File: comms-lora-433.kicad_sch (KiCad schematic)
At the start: 3 parts, among them J3 Conn_Coaxial_Small, U3 RFM95W-915S2

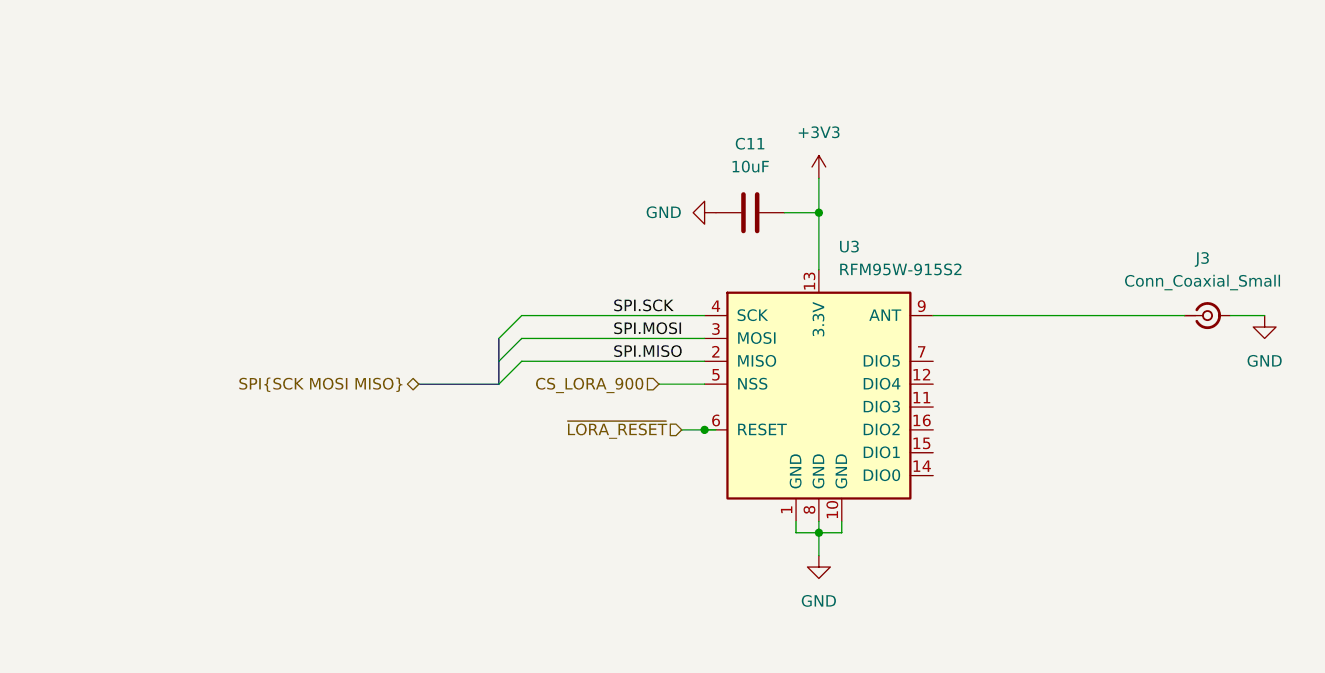
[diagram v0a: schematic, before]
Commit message: Adding symbols information
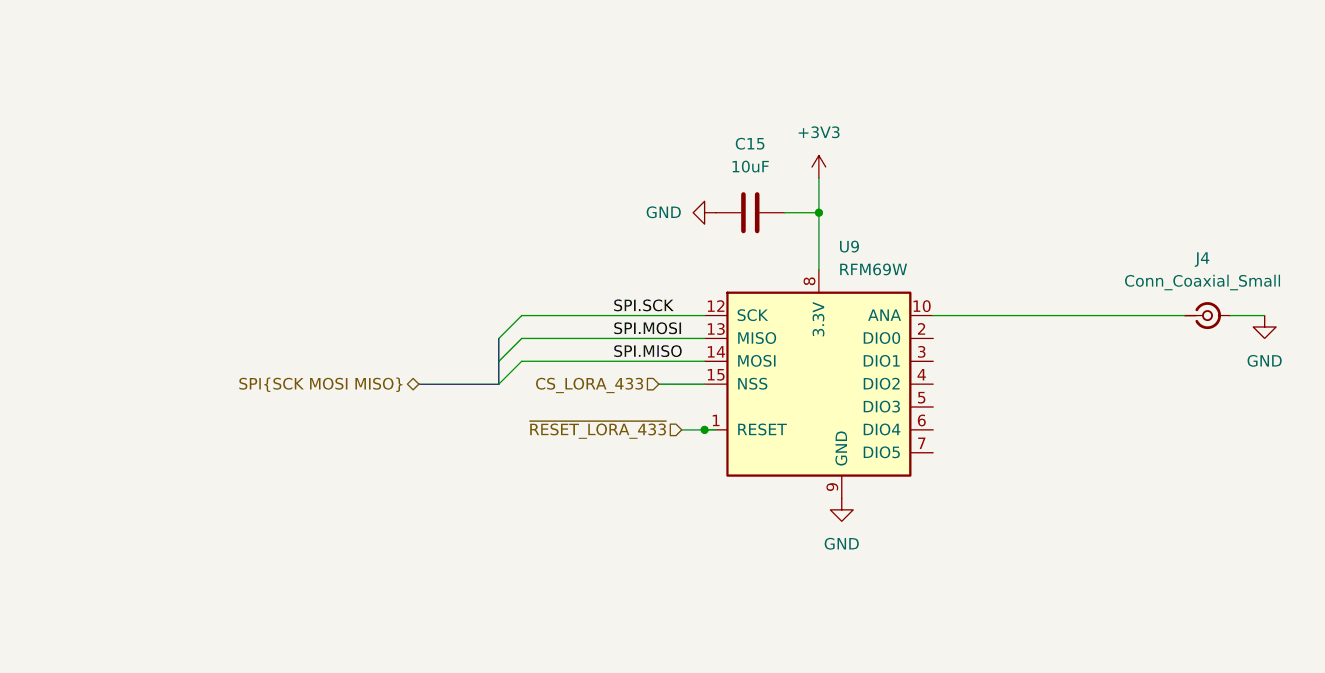
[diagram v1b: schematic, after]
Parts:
- removed U3: RFM95W-915S2, symbol RF_Module:RFM95W-915S2
- added U9: RFM69W, RF_Module:HOPERF_RFM69HW, symbol RF_Module:RFM69W
- renumbered C11 to C15, J3 to J4
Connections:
- net +3V3: now also U9.8 (3.3V)
- net GND: now also U9.11 (GND), U9.9 (GND)
- net SPI.MISO: now also U9.14 (MOSI)
- net SPI.MOSI: now also U9.13 (MISO)
- net SPI.SCK: now also U9.12 (SCK)
- net at J4.1 (In): now also U9.10 (ANA)
- new net CS_LORA_433: U9.15 (NSS)
- new net ~{RESET_LORA_433}: U9.1 (RESET)
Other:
- company: (none) -> catbranchman

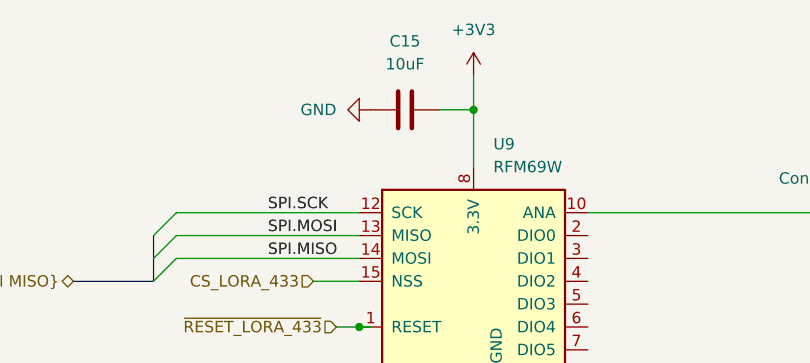
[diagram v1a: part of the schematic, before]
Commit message: Adding rest of schematic
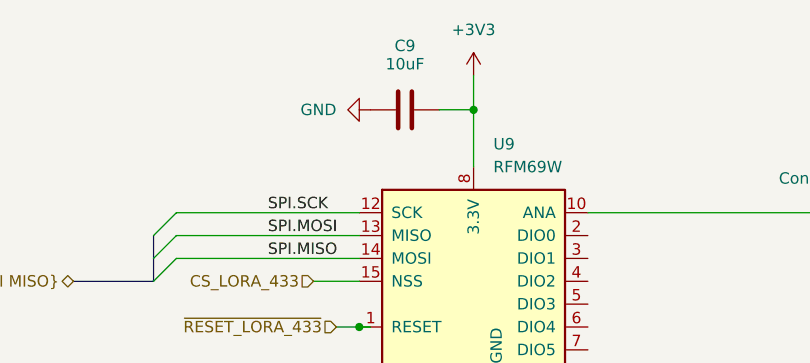
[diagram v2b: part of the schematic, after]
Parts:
- removed C15: 10uF, symbol Device:C
- added C9: 10uF, Inductor_SMD:L_0805_2012Metric, symbol Device:C
- J4: footprint (none) -> Connector_Coaxial:U.FL_Molex_MCRF_73412-0110_Vertical; Mfr (none) -> Molex; Mfr P/N (none) -> 0734120110; Supplier_1 (none) -> Digikey; Supplier_1 P/N (none) -> WM5587CT-ND; Supplier_1 Price @ Qty (none) -> $0.38945; Supplier_1 Unit Price (none) -> $0.94000
- U9: Mfr (none) -> Adafruit; Mfr P/N (none) -> 3073; Supplier_1 (none) -> Adafruit; Supplier_1 P/N (none) -> 3073; Supplier_1 Price @ Qty (none) -> $15.96; Supplier_1 Unit Price (none) -> $19.95
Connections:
- net +3V3: now also C9.2
- net GND: now also C9.1

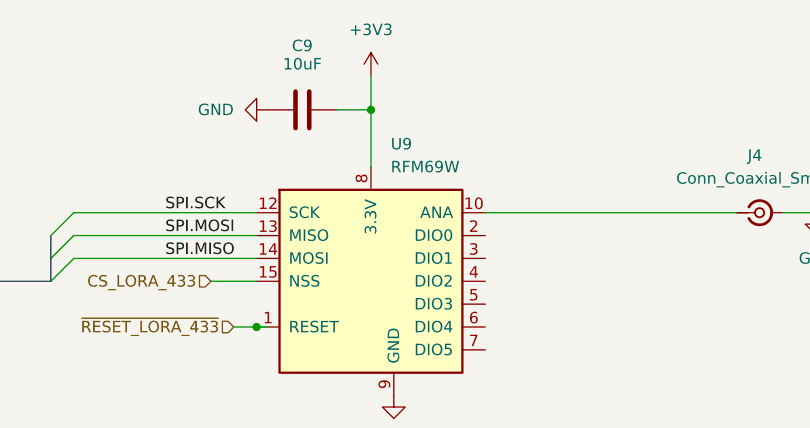
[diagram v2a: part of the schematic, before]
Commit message: Fixing footprint imports
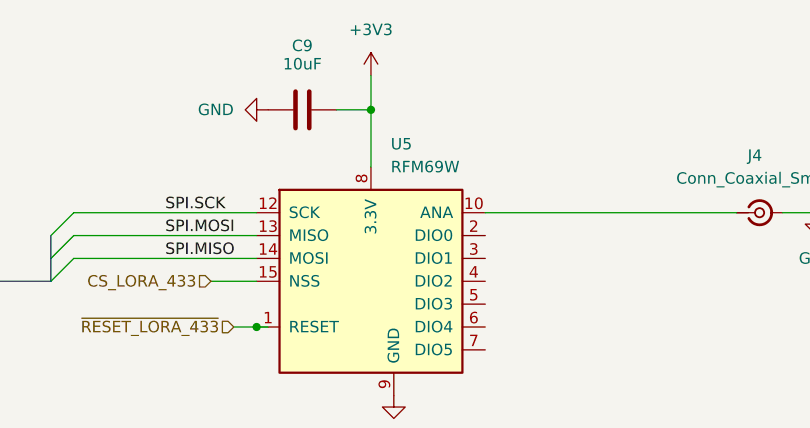
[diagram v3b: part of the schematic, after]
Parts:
- renumbered U9 to U5
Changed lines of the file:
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@@
 		)
 	)
-	(label "SPI.MOSI"
-		(at 121.92 92.71 0)
+	(label "SPI.MISO"
+		(at 121.92 95.25 0)
 		(fields_autoplaced yes)
 		(effects
@@
 		)
 	)
-	(label "SPI.MISO"
-		(at 121.92 95.25 0)
+	(label "SPI.MOSI"
+		(at 121.92 92.71 0)
 		(fields_autoplaced yes)
 		(effects
@@
 		)
 	)
+	(hierarchical_label "~{RESET_LORA_433}"
+		(shape input)
+		(at 129.54 102.87 180)
+		(fields_autoplaced yes)
+		(effects
+			(font
+				(size 1.27 1.27)
+			)
+			(justify right)
+		)
+	)
 	(hierarchical_label "CS_LORA_433"
 		(shape input)
 		(at 127 97.79 180)
-		(fields_autoplaced yes)
-		(effects
-			(font
-				(size 1.27 1.27)
-			)
-			(justify right)
-		)
-	)
-	(hierarchical_label "~{RESET_LORA_433}"
-		(shape input)
-		(at 129.54 102.87 180)
 		(fields_autoplaced yes)
 		(effects
@@
 		(dnp no)
 		(fields_autoplaced yes)
-		(property "Reference" "U9"
+		(property "Reference" "U5"
 			(at 146.9741 82.55 0)
 			(effects
@@
 			(project ""
 				(path "/1c59de6a-87fe-4223-8898-4b0383164a31/27e0c772-2e0b-4398-8c51-a65e2e356334"
-					(reference "U9")
+					(reference "U5")
+					(unit 1)
+				)
+			)
+		)
+	)
+	(symbol
+		(lib_id "power:GND")
+		(at 133.35 78.74 270)
+		(unit 1)
+		(exclude_from_sim no)
+		(in_bom yes)
+		(on_board yes)
+		(dnp no)
+		(fields_autoplaced yes)
+		(property "Reference" "#PWR058"
+			(at 127 78.74 0)
+			(effects
+				(font
+					(size 1.27 1.27)
+				)
+				(hide yes)
+			)
+		)
+		(property "Value" "GND"
+			(at 129.54 78.7399 90)
+			(effects
+				(font
+					(size 1.27 1.27)
+				)
+				(justify right)
+			)
+		)
+		(property "Footprint" ""
+			(at 133.35 78.74 0)
+			(effects
+				(font
+					(size 1.27 1.27)
+				)
+				(hide yes)
+			)
+		)
+		(property "Datasheet" ""
+			(at 133.35 78.74 0)
+			(effects
+				(font
+					(size 1.27 1.27)
+				)
+				(hide yes)
+			)
+		)
+		(property "Description" "Power symbol creates a global label with name \"GND\" , ground"
+			(at 133.35 78.74 0)
+			(effects
+				(font
+					(size 1.27 1.27)
+				)
+				(hide yes)
+			)
+		)
+		(pin "1"
+		)
+		(instances
+			(project "roamer"
+				(path "/1c59de6a-87fe-4223-8898-4b0383164a31/27e0c772-2e0b-4398-8c51-a65e2e356334"
+					(reference "#PWR058")
 					(unit 1)
 				)
@@
 	)
 	(symbol
-		(lib_id "power:GND")
-		(at 133.35 78.74 270)
-		(unit 1)
-		(exclude_from_sim no)
-		(in_bom yes)
-		(on_board yes)
-		(dnp no)
-		(fields_autoplaced yes)
-		(property "Reference" "#PWR058"
-			(at 127 78.74 0)
-			(effects
-				(font
-					(size 1.27 1.27)
-				)
-				(hide yes)
-			)
-		)
-		(property "Value" "GND"
-			(at 129.54 78.7399 90)
-			(effects
-				(font
-					(size 1.27 1.27)
-				)
-				(justify right)
-			)
-		)
-		(property "Footprint" ""
-			(at 133.35 78.74 0)
-			(effects
-				(font
-					(size 1.27 1.27)
-				)
-				(hide yes)
-			)
-		)
-		(property "Datasheet" ""
-			(at 133.35 78.74 0)
-			(effects
-				(font
-					(size 1.27 1.27)
-				)
-				(hide yes)
-			)
-		)
-		(property "Description" "Power symbol creates a global label with name \"GND\" , ground"
-			(at 133.35 78.74 0)
-			(effects
-				(font
-					(size 1.27 1.27)
-				)
-				(hide yes)
-			)
-		)
-		(pin "1"
-		)
-		(instances
-			(project "roamer"
-				(path "/1c59de6a-87fe-4223-8898-4b0383164a31/27e0c772-2e0b-4398-8c51-a65e2e356334"
-					(reference "#PWR058")
-					(unit 1)
-				)
-			)
-		)
-	)
-	(symbol
 		(lib_id "power:+3V3")
 		(at 144.78 74.93 0)
@@
 				(path "/1c59de6a-87fe-4223-8898-4b0383164a31/27e0c772-2e0b-4398-8c51-a65e2e356334"
 					(reference "#PWR059")
+					(unit 1)
+				)
+			)
+		)
+	)
+	(symbol
+		(lib_id "power:GND")
+		(at 194.31 90.17 0)
+		(unit 1)
+		(exclude_from_sim no)
+		(in_bom yes)
+		(on_board yes)
+		(dnp no)
+		(fields_autoplaced yes)
+		(property "Reference" "#PWR061"
+			(at 194.31 96.52 0)
+			(effects
+				(font
+					(size 1.27 1.27)
+				)
+				(hide yes)
+			)
+		)
+		(property "Value" "GND"
+			(at 194.31 95.25 0)
+			(effects
+				(font
+					(size 1.27 1.27)
+				)
+			)
+		)
+		(property "Footprint" ""
+			(at 194.31 90.17 0)
+			(effects
+				(font
+					(size 1.27 1.27)
+				)
+				(hide yes)
+			)
+		)
+		(property "Datasheet" ""
+			(at 194.31 90.17 0)
+			(effects
+				(font
+					(size 1.27 1.27)
+				)
+				(hide yes)
+			)
+		)
+		(property "Description" "Power symbol creates a global label with name \"GND\" , ground"
+			(at 194.31 90.17 0)
+			(effects
+				(font
+					(size 1.27 1.27)
+				)
+				(hide yes)
+			)
+		)
+		(pin "1"
+		)
+		(instances
+			(project "roamer"
+				(path "/1c59de6a-87fe-4223-8898-4b0383164a31/27e0c772-2e0b-4398-8c51-a65e2e356334"
+					(reference "#PWR061")
 					(unit 1)
 				)
@@
 					(unit 1)
 				)
-			)
-		)
-	)
-	(symbol
-		(lib_id "power:GND")
-		(at 194.31 90.17 0)
-		(unit 1)
-		(exclude_from_sim no)
-		(in_bom yes)
-		(on_board yes)
-		(dnp no)
-		(fields_autoplaced yes)
-		(property "Reference" "#PWR061"
-			(at 194.31 96.52 0)
-			(effects
-				(font
-					(size 1.27 1.27)
-				)
-				(hide yes)
-			)
-		)
-		(property "Value" "GND"
-			(at 194.31 95.25 0)
-			(effects
-				(font
-					(size 1.27 1.27)
-				)
-			)
-		)
-		(property "Footprint" ""
-			(at 194.31 90.17 0)
-			(effects
-				(font
-					(size 1.27 1.27)
-				)
-				(hide yes)
-			)
-		)
-		(property "Datasheet" ""
-			(at 194.31 90.17 0)
-			(effects
-				(font
-					(size 1.27 1.27)
-				)
-				(hide yes)
-			)
-		)
-		(property "Description" "Power symbol creates a global label with name \"GND\" , ground"
-			(at 194.31 90.17 0)
-			(effects
-				(font
-					(size 1.27 1.27)
-				)
-				(hide yes)
-			)
-		)
-		(pin "1"
-		)
-		(instances
-			(project "roamer"
-				(path "/1c59de6a-87fe-4223-8898-4b0383164a31/27e0c772-2e0b-4398-8c51-a65e2e356334"
-					(reference "#PWR061")
-					(unit 1)
-				)

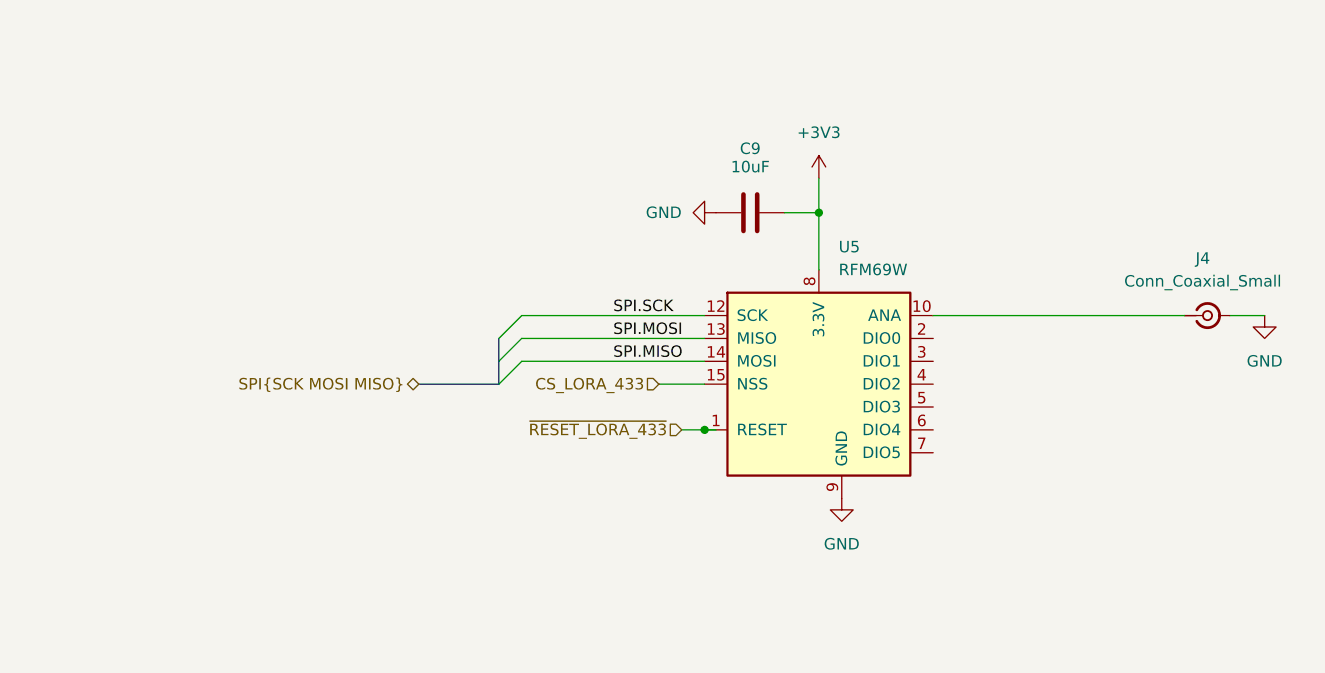
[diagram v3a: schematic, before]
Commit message: Spamming 0 ohm resistors
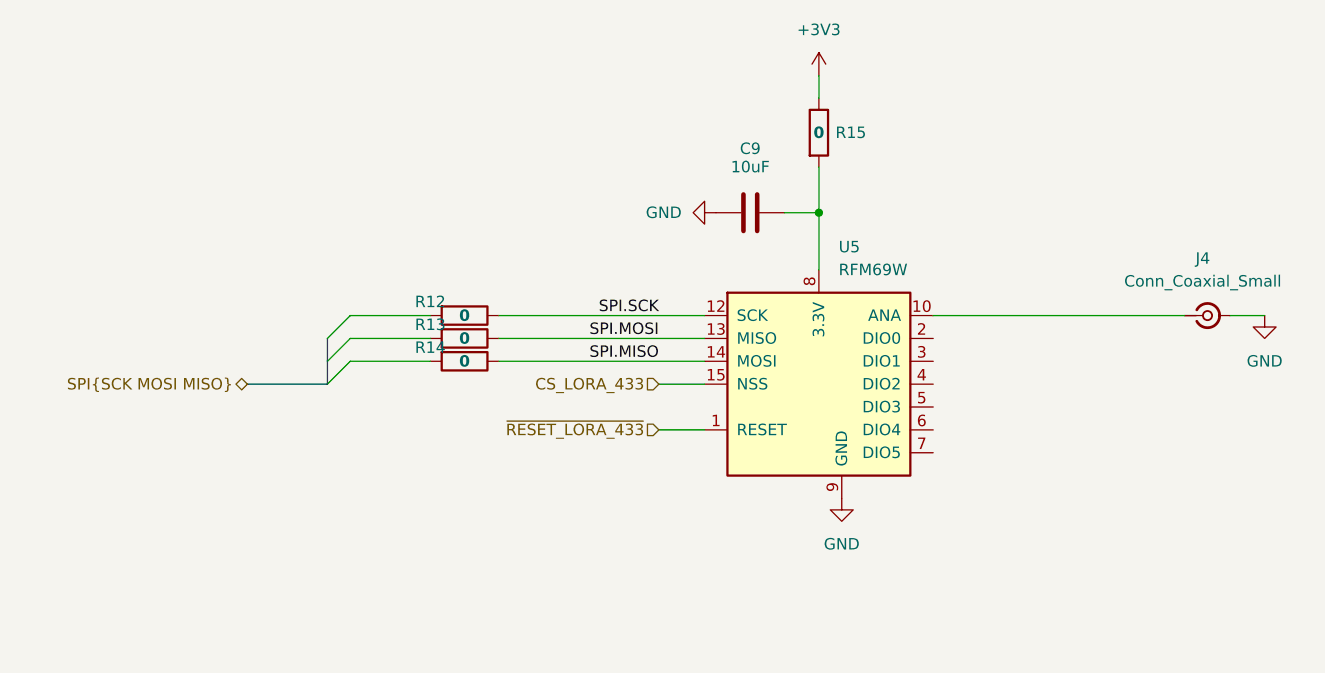
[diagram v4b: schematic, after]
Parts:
- added R12, R13, R14, R15: 0, Resistor_SMD:R_0603_1608Metric, symbol Device:R
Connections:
- net +3V3: now also R15.1; no longer C9.2, U5.8 (3.3V)
- net SPI.MISO: now also R14.1
- net SPI.MOSI: now also R13.1
- net SPI.SCK: now also R12.1
- new net: C9.2, R15.2, U5.8 (3.3V)
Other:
- title: (none) -> Comms - LoRa 433

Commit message: Adding more 0 ohm resistors and pullups for I2C lines
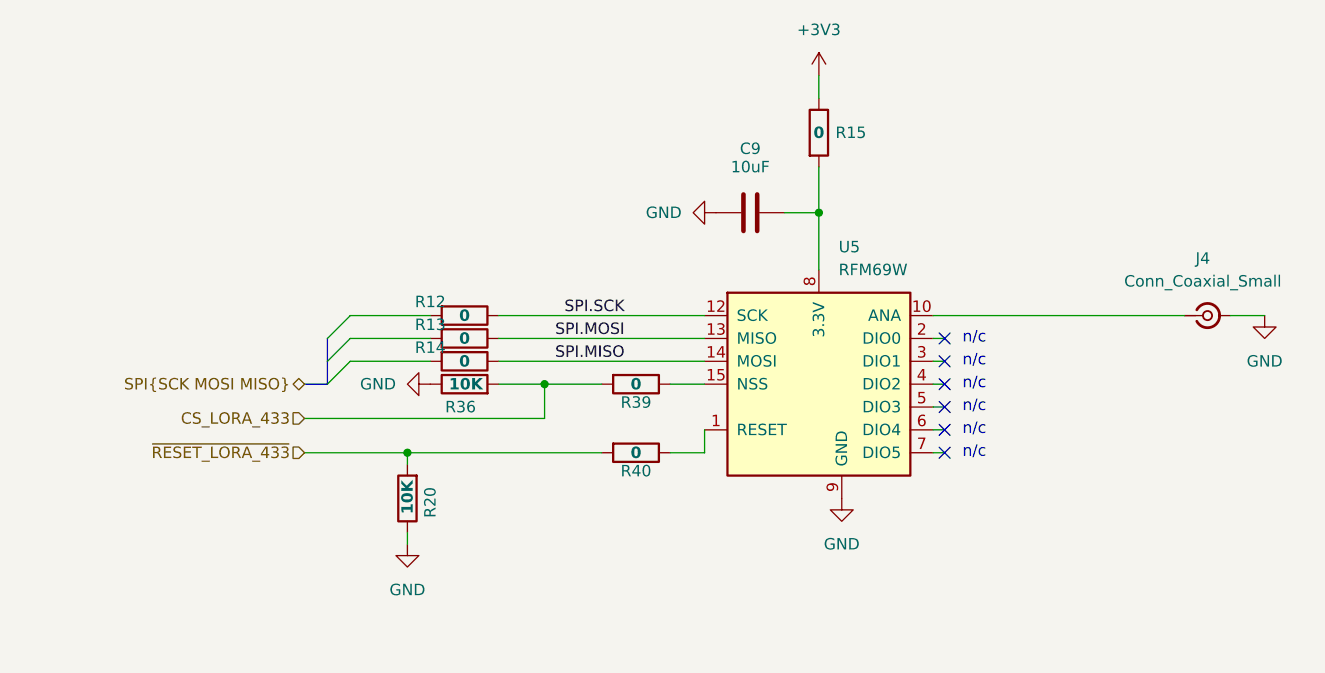
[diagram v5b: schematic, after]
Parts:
- added R20, R36: 10K, Resistor_SMD:R_0603_1608Metric, symbol Device:R
- added R39, R40: 0, Resistor_SMD:R_0603_1608Metric, symbol Device:R
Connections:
- net CS_LORA_433: now also R36.2, R39.2; no longer U5.15 (NSS)
- net GND: now also R20.1, R36.1
- net ~{RESET_LORA_433}: now also R20.2, R40.2; no longer U5.1 (RESET)
- new net: R40.1, U5.1 (RESET)
- new net: R39.1, U5.15 (NSS)
- no-connect marks 0 -> 6
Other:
- note added: "n/c"

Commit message: Adding testpoints to I2C, SPI, and signals
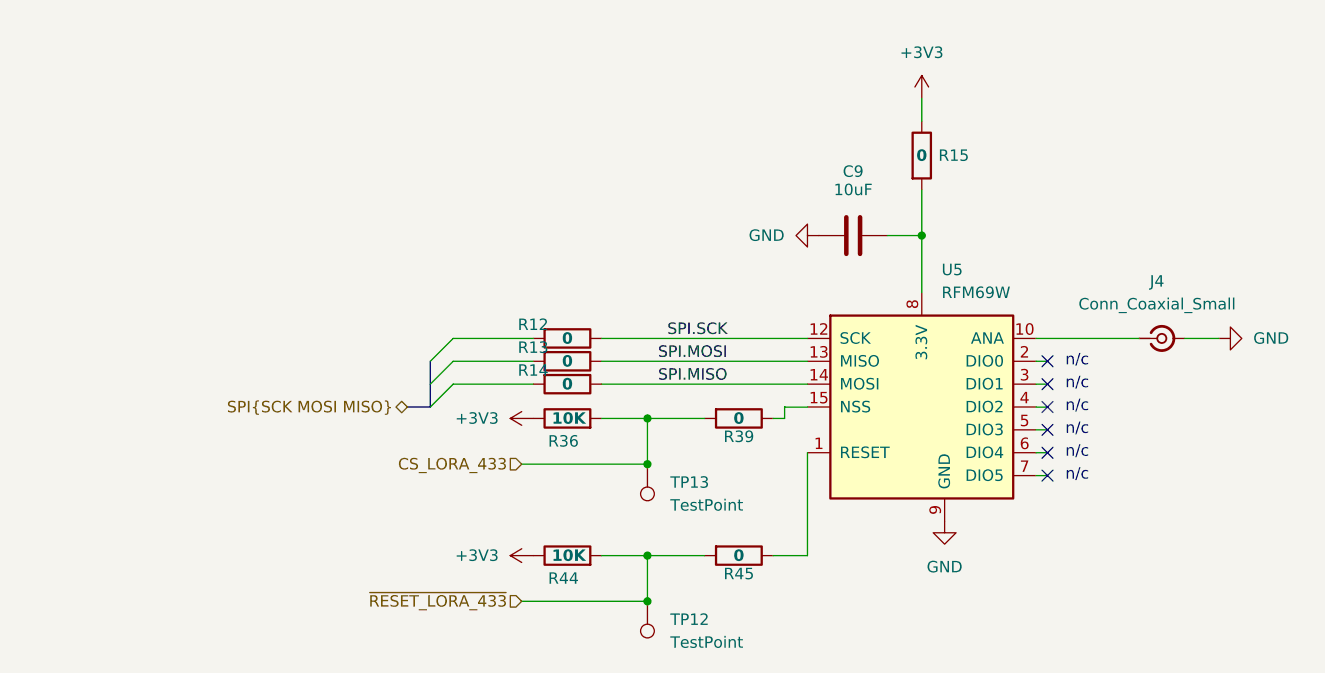
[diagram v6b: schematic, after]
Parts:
- removed R20: 10K, Resistor_SMD:R_0603_1608Metric, symbol Device:R
- removed R40: 0, Resistor_SMD:R_0603_1608Metric, symbol Device:R
- added R44: 10K, Resistor_SMD:R_0603_1608Metric, symbol Device:R
- added R45: 0, Resistor_SMD:R_0603_1608Metric, symbol Device:R
- added TP12, TP13: TestPoint, TestPoint:TestPoint_Loop_D2.50mm_Drill1.0mm, symbol Connector:TestPoint
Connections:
- net +3V3: now also R36.1, R44.1
- net CS_LORA_433: now also TP13.1
- net GND: no longer R36.1
- net ~{RESET_LORA_433}: now also R44.2, R45.2, TP12.1
- net at U5.1 (RESET): now also R45.1
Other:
- moved on the sheet: C9, J4, R12, R13, R14, R15, R36, R39, U5
